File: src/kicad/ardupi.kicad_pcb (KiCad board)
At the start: 2 copper layers, 65 x 56 mm, 54 parts, among them J1 GPIO, J10 Conn_01x04, J11 TSW-108-08-L-T-RA, J2 Conn_01x10, J3 Conn_01x05, J4 Conn_01x04, J6 Conn_01x05, J7 Conn_01x06, J8 Conn_01x04, J9 Conn_01x02, U1 CAT24C256, U2 ULN2803ADW, U3 PCA9685BS, U4 ADS1115IRUGR, U5 MPU-9250, U6 BMP280

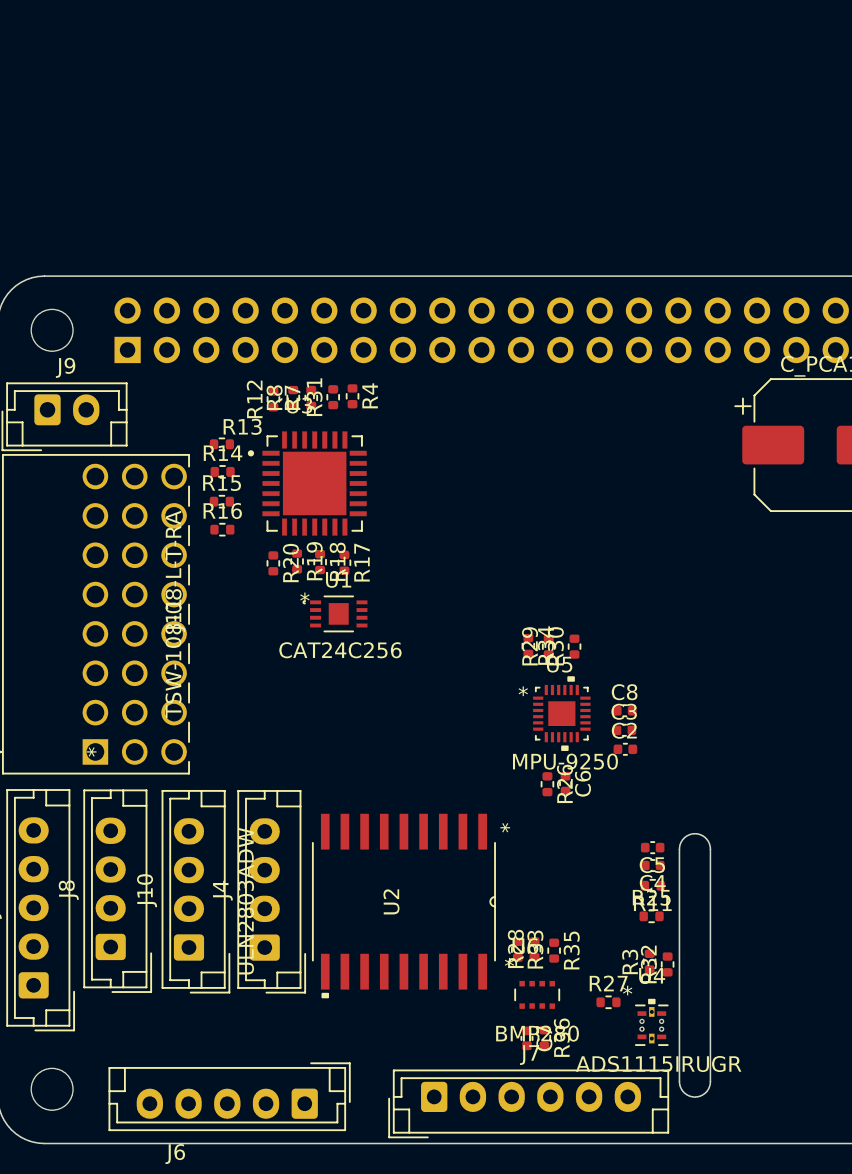
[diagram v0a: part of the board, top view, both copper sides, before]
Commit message: +ADS1115IDGSR update all symbol footprints VSS = GND
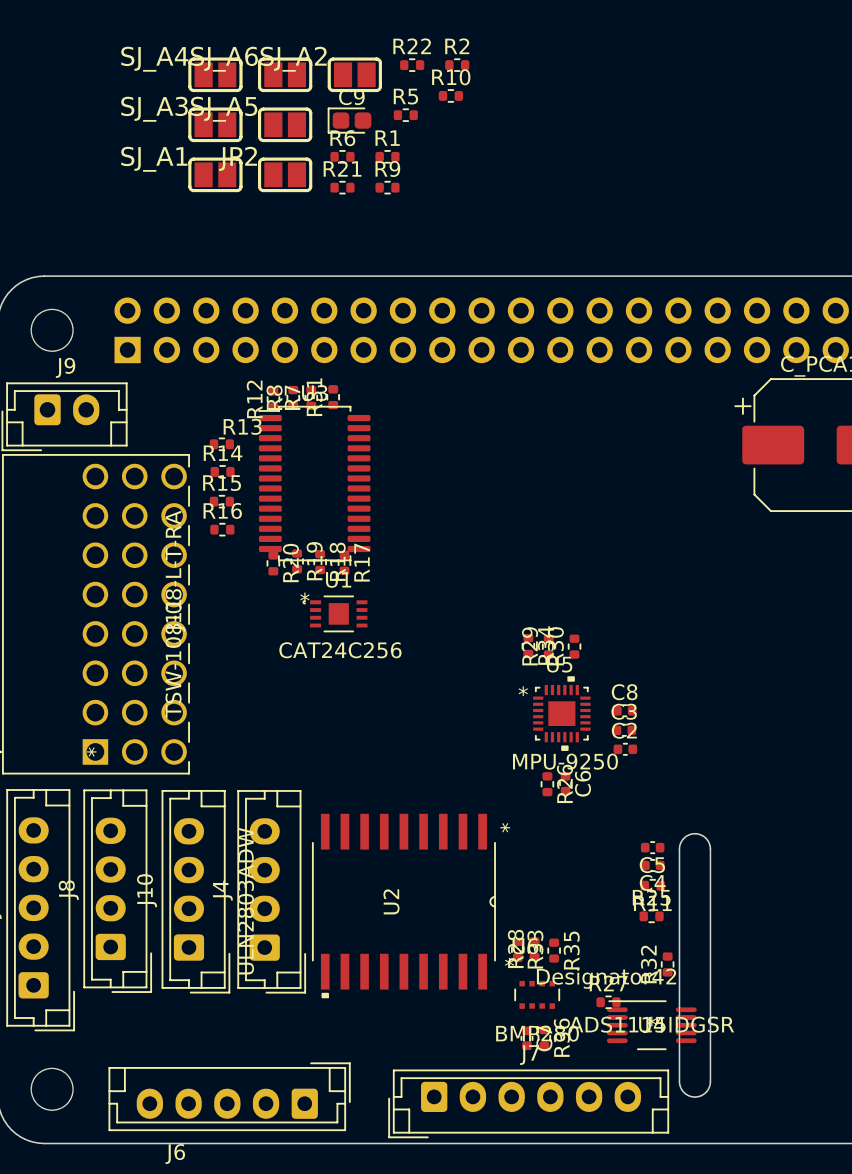
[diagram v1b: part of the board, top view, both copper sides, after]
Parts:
- removed R3, R4: 10k, Resistor_SMD:R_0402_1005Metric
- added C9: 100n, Capacitor_Tantalum_SMD:CP_EIA-1608-10_AVX-L, F.Cu at (122.9, 34.0)
- added JP2: ID_WP, Ardupi:SOLDERJUMPER_REFLOW_NOPASTE, F.Cu at (118.5, 37.5)
- added R1: 10k, Resistor_SMD:R_0402_1005Metric, F.Cu at (125.2, 36.3)
- added R10: 10k, Resistor_SMD:R_0402_1005Metric, F.Cu at (129.2, 32.4)
- added R2: 10k, Resistor_SMD:R_0402_1005Metric, F.Cu at (129.7, 30.4)
- added R21: 3.9k, Resistor_SMD:R_0402_1005Metric, F.Cu at (122.2, 38.3)
- added R22: 3.9k, Resistor_SMD:R_0402_1005Metric, F.Cu at (126.7, 30.4)
- added R5: 10k, Resistor_SMD:R_0402_1005Metric, F.Cu at (126.3, 33.6)
- added R6: 10K, Resistor_SMD:R_0402_1005Metric, F.Cu at (122.2, 36.3)
- added R9: 10k, Resistor_SMD:R_0402_1005Metric, F.Cu at (125.2, 38.3)
- added SJ_A1: SOLDERJUMPERREFLOW_NOPASTE, Ardupi:SOLDERJUMPER_REFLOW_NOPASTE, F.Cu at (114.0, 37.5)
- added SJ_A2: SOLDERJUMPERREFLOW_NOPASTE, Ardupi:SOLDERJUMPER_REFLOW_NOPASTE, F.Cu at (123.0, 31.0)
- added SJ_A3: SOLDERJUMPERREFLOW_NOPASTE, Ardupi:SOLDERJUMPER_REFLOW_NOPASTE, F.Cu at (114.0, 34.2)
- added SJ_A4: SOLDERJUMPERREFLOW_NOPASTE, Ardupi:SOLDERJUMPER_REFLOW_NOPASTE, F.Cu at (114.0, 31.0)
- added SJ_A5: SOLDERJUMPERREFLOW_NOPASTE, Ardupi:SOLDERJUMPER_REFLOW_NOPASTE, F.Cu at (118.5, 34.2)
- added SJ_A6: SOLDERJUMPERREFLOW_NOPASTE, Ardupi:SOLDERJUMPER_REFLOW_NOPASTE, F.Cu at (118.5, 31.0)
- J1: value GPIO -> RPI-4B-Header
- U3: value PCA9685BS -> PCA9685PW; footprint Ardupi:PCA9685BS_118 -> Package_SO:TSSOP-28_4.4x9.7mm_P0.65mm
- U4: value ADS1115IRUGR -> ADS1115IDGSR; footprint Ardupi:ADS1115IRUGT -> Ardupi:ADS1115IDGSR
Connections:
- J1 pad 27: /ID_SDA -> unconnected-(J1-Pad27)
- J1 pad 28: /ID_SCL -> unconnected-(J1-Pad28)
- R32 pad 1: /SDA1 -> +5V
- R32 pad 2: +5V -> /SDA1
- U3 pad 1: unconnected-(U3-Pad1) -> Net-(R5-Pad1)
- U3 pad 10: /PWM7 -> /PWM5
- U3 pad 11: unconnected-(U3-Pad11) -> /PWM6
- U3 pad 12: /PWM8 -> /PWM7
- U3 pad 13: /PWM9 -> /PWM8
- U3 pad 14: /PWM10 -> GND
- U3 pad 15: /PWM11 -> /PWM9
- U3 pad 16: /PWM12 -> /PWM10
- U3 pad 17: /PWM13 -> /PWM11
- U3 pad 18: /PWM14 -> /PWM12
- U3 pad 19: /PWM15 -> /PWM13
- U3 pad 2: unconnected-(U3-Pad2) -> Net-(R6-Pad1)
- U3 pad 20: unconnected-(U3-Pad20) -> /PWM14
- U3 pad 21: unconnected-(U3-Pad21) -> /PWM15
- U3 pad 22: /SCL1 -> /PWM16
- U3 pad 23: Net-(R7-Pad1) -> /PCA_EN
- U3 pad 24: Net-(R8-Pad1) -> Net-(R10-Pad1)
- U3 pad 25: unconnected-(U3-Pad25) -> GND
- U3 pad 26: /PCA_EN -> /SCL1
- U3 pad 27: unconnected-(U3-Pad27) -> /SDA1
- U3 pad 28: unconnected-(U3-Pad28) -> +5V
- U3 pad 3: unconnected-(U3-Pad3) -> Net-(R7-Pad1)
- U3 pad 4: /PWM1 -> Net-(R8-Pad1)
- U3 pad 5: /PWM2 -> Net-(R9-Pad1)
- U3 pad 6: /PWM3 -> /PWM1
- U3 pad 7: /PWM4 -> /PWM2
- U3 pad 8: /PWM5 -> /PWM3
- U3 pad 9: /PWM6 -> /PWM4
- U4 pad 10: /SCL1 -> /AIO2
- U4 pad 6: /AIO2 -> /SCL1
- U4 pad 9: /SDA1 -> /AIO3
- U5 pad 18: unconnected-(U5-Pad18) -> GND

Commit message: schematic version bump
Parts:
- U1: value CAT24C256 -> CAT24C256HU4IGT3
- U2: value ULN2803ADW -> ULN2803ADWR
- U3: footprint Package_SO:TSSOP-28_4.4x9.7mm_P0.65mm -> Ardupi:PCA9685PW_118
- moved SJ_A2 158.3 mm to (39.6, 165.6)
- moved R10 155.4 mm to (53.2, 167.9)
- moved C9 155.2 mm to (43.9, 167.6)
- moved R21 154.4 mm to (38.8, 168.2)
- moved R1 151.4 mm to (50.3, 167.9)
- moved R5 146.4 mm to (64.9, 166.5)
- moved SJ_A4 144.2 mm to (53.9, 162.0)
- moved JP2 143.2 mm to (53.9, 165.3)
- moved R8 135.8 mm to (47.4, 167.3), turned to 0 degrees
- moved J2 135.2 mm to (33.5, 126.2), turned to 0 degrees
- moved U4 131.3 mm to (33.7, 166.3)
- moved R22 130.0 mm to (78.5, 151.1)
- moved R9 129.8 mm to (69.5, 155.6)
- moved U3 129.7 mm to (36.4, 156.2)
- moved J9 124.5 mm to (45.6, 163.1)
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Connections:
- J1 pad 1: +3V3 -> unconnected-(J1-Pad1)
- J1 pad 11: /SRVO_EN -> unconnected-(J1-Pad11)
- J1 pad 13: /LED1 -> unconnected-(J1-Pad13)
- J1 pad 15: /LED2 -> unconnected-(J1-Pad15)
- J1 pad 17: +3V3 -> unconnected-(J1-Pad17)
- J1 pad 19: /SPI_MOSI -> unconnected-(J1-Pad19)
- J1 pad 21: /SPI_MISO -> unconnected-(J1-Pad21)
- J1 pad 23: /SPI_SCLK -> unconnected-(J1-Pad23)
- J1 pad 25: GND -> unconnected-(J1-Pad25)
- J1 pad 28: unconnected-(J1-Pad28) -> /ID_SCL
- J1 pad 29: /RC1 -> unconnected-(J1-Pad29)
- J1 pad 3: /SDA1 -> unconnected-(J1-Pad3)
- J1 pad 31: /RC2 -> unconnected-(J1-Pad31)
- J1 pad 33: /RC3 -> unconnected-(J1-Pad33)
- J1 pad 35: /RC4 -> unconnected-(J1-Pad35)
- J1 pad 37: /RC5 -> unconnected-(J1-Pad37)
- J1 pad 39: GND -> unconnected-(J1-Pad39)
- J1 pad 5: /SCL1 -> unconnected-(J1-Pad5)
- J1 pad 7: /LED3 -> unconnected-(J1-Pad7)
- J1 pad 9: GND -> unconnected-(J1-Pad9)

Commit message: +NEO-M8Q-01A module
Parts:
- removed C2, C6: 0.1uF, Capacitor_SMD:C_0402_1005Metric
- removed C3, C4, C8: 1uF, Capacitor_SMD:C_0402_1005Metric
- removed C5: 0.1uf, Capacitor_SMD:C_0402_1005Metric
- removed C7: 0.01uF, Capacitor_SMD:C_0402_1005Metric
- removed C9: 100n, Capacitor_Tantalum_SMD:CP_EIA-1608-10_AVX-L
- removed C_PCA1: 10uF, Capacitor_SMD:CP_Elec_8x5.4
- removed J10, J4, J8: Conn_01x04, Connector_JST:JST_EH_B4B-EH-A_1x04_P2.50mm_Vertical
- removed J11: TSW-108-08-L-T-RA, Ardupi:TSW-108-08-L-T-RA
- removed J2: Conn_01x10, Connector_JST:JST_EH_B10B-EH-A_1x10_P2.50mm_Vertical
- removed J3, J6: Conn_01x05, Connector_JST:JST_EH_B5B-EH-A_1x05_P2.50mm_Vertical
- removed J7: Conn_01x06, Connector_JST:JST_EH_B6B-EH-A_1x06_P2.50mm_Vertical
- removed J9: Conn_01x02, Connector_JST:JST_EH_B2B-EH-A_1x02_P2.50mm_Vertical
- removed JP2: ID_WP, Ardupi:SOLDERJUMPER_REFLOW_NOPASTE
- removed R1, R10, R2, R5, R9: 10k, Resistor_SMD:R_0402_1005Metric
- removed R11, R6, R7, R8: 10K, Resistor_SMD:R_0402_1005Metric
- removed R12: 460, Resistor_SMD:R_0402_1005Metric
- removed R13, R14, R15, R16, R17, R18, R19, R20: 220 Ω, Resistor_SMD:R_0402_1005Metric
- removed R21, R22: 3.9k, Resistor_SMD:R_0402_1005Metric
- removed R25, R26, R27, R28, R31, R32, R36: 10KΩ, Resistor_SMD:R_0402_1005Metric
- removed R29, R30, R33, R34, R35: 4.7KΩ, Resistor_SMD:R_0402_1005Metric
- removed SJ_A1, SJ_A2, SJ_A3, SJ_A4, SJ_A5, SJ_A6: SOLDERJUMPERREFLOW_NOPASTE, Ardupi:SOLDERJUMPER_REFLOW_NOPASTE
- removed U1: CAT24C256HU4IGT3, Ardupi:CAT24C256HU4IGT3
- removed U2: ULN2803ADWR, Ardupi:ULN2803ADWR
- removed U3: PCA9685PW, Ardupi:PCA9685PW_118
- removed U4: ADS1115IDGSR, Ardupi:ADS1115IDGSR
- removed U5: MPU-9250, Ardupi:mpu9250
- removed U6: BMP280, Ardupi:bmp280
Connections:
- J1 pad 1: unconnected-(J1-Pad1) -> +3V3
- J1 pad 11: unconnected-(J1-Pad11) -> /SRVO_EN
- J1 pad 13: unconnected-(J1-Pad13) -> /LED1
- J1 pad 15: unconnected-(J1-Pad15) -> /LED2
- J1 pad 17: unconnected-(J1-Pad17) -> +3V3
- J1 pad 19: unconnected-(J1-Pad19) -> /SPI_MOSI
- J1 pad 21: unconnected-(J1-Pad21) -> /SPI_MISO
- J1 pad 23: unconnected-(J1-Pad23) -> /SPI_SCLK
- J1 pad 25: unconnected-(J1-Pad25) -> GND
- J1 pad 27: unconnected-(J1-Pad27) -> /ID_SD
- J1 pad 28: /ID_SCL -> /ID_SC
- J1 pad 29: unconnected-(J1-Pad29) -> /RC1
- J1 pad 3: unconnected-(J1-Pad3) -> /SDA1
- J1 pad 31: unconnected-(J1-Pad31) -> /RC2
- J1 pad 33: unconnected-(J1-Pad33) -> /RC3
- J1 pad 35: unconnected-(J1-Pad35) -> /RC4
- J1 pad 37: unconnected-(J1-Pad37) -> /RC5
- J1 pad 39: unconnected-(J1-Pad39) -> GND
- J1 pad 5: unconnected-(J1-Pad5) -> /SCL1
- J1 pad 7: unconnected-(J1-Pad7) -> /LED3
- J1 pad 9: unconnected-(J1-Pad9) -> GND

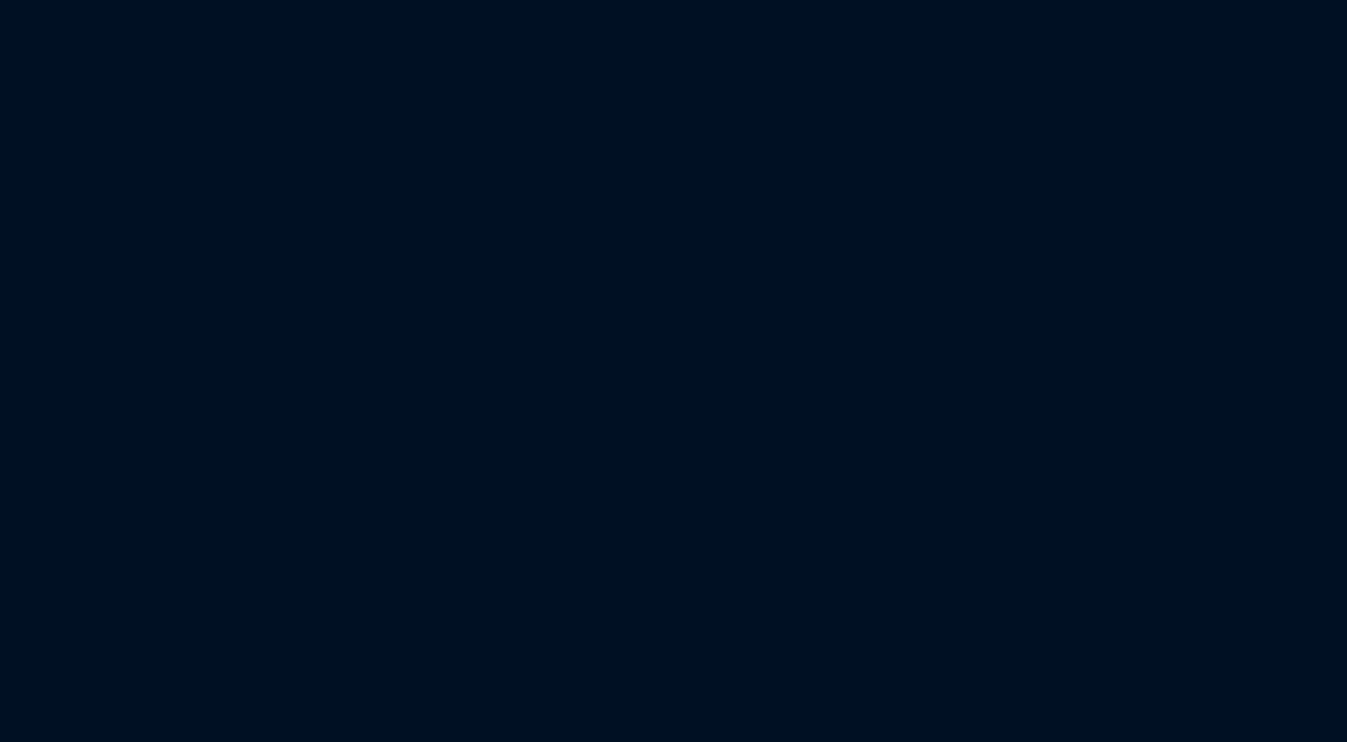
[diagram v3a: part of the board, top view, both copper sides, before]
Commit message: + expresslrs.
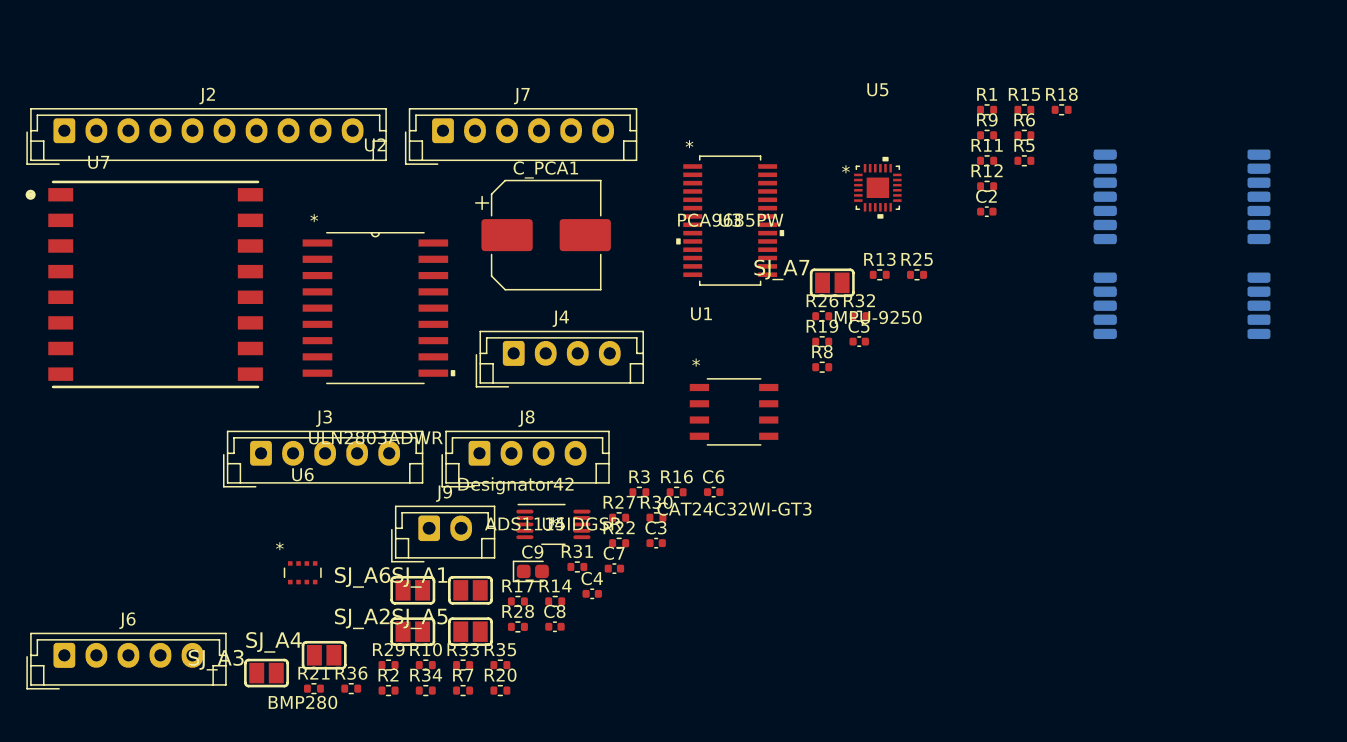
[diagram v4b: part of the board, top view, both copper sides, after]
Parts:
- added C2: 0.1uF, Capacitor_SMD:C_0402_1005Metric, F.Cu at (112.7, 133.0)
- added C3: 1uF, Capacitor_SMD:C_0402_1005Metric, F.Cu at (86.9, 158.9)
- added C4: 1uF, Capacitor_SMD:C_0402_1005Metric, F.Cu at (81.9, 162.8)
- added C5: 0.1uf, Capacitor_SMD:C_0402_1005Metric, F.Cu at (102.7, 143.2)
- added C6: 0.1uF, Capacitor_SMD:C_0402_1005Metric, F.Cu at (91.4, 154.9)
- added C7: 0.01uF, Capacitor_SMD:C_0402_1005Metric, F.Cu at (83.6, 160.9)
- added C8: 1uF, Capacitor_SMD:C_0402_1005Metric, F.Cu at (79.0, 165.4)
- added C9: 100n, Capacitor_Tantalum_SMD:CP_EIA-1608-10_AVX-L, F.Cu at (77.3, 161.1)
- added C_PCA1: 10uF, Capacitor_SMD:CP_Elec_8x5.4, F.Cu at (78.3, 134.8)
- added J2: Conn_01x10, Connector_JST:JST_EH_B10B-EH-A_1x10_P2.50mm_Vertical, F.Cu at (40.7, 126.7)
- added J3: Conn_01x05, Connector_JST:JST_EH_B5B-EH-A_1x05_P2.50mm_Vertical, F.Cu at (56.0, 151.9)
- added J4: Conn_01x04, Connector_JST:JST_EH_B4B-EH-A_1x04_P2.50mm_Vertical, F.Cu at (75.8, 144.1)
- added J6: Conn_01x05, Connector_JST:JST_EH_B5B-EH-A_1x05_P2.50mm_Vertical, F.Cu at (40.7, 167.7)
- added J7: Conn_01x06, Connector_JST:JST_EH_B6B-EH-A_1x06_P2.50mm_Vertical, F.Cu at (70.2, 126.7)
- added J8: Conn_01x04, Connector_JST:JST_EH_B4B-EH-A_1x04_P2.50mm_Vertical, F.Cu at (73.1, 151.9)
- added J9: Conn_01x02, Connector_JST:JST_EH_B2B-EH-A_1x02_P2.50mm_Vertical, F.Cu at (69.2, 157.7)
- added M1: NEO-M8Q-01A, Ardupi:ublox_NEO, B.Cu at (127.9, 135.6)
- added R1: 10k, Resistor_SMD:R_0402_1005Metric, F.Cu at (112.7, 125.1)
- added R10: 10k, Resistor_SMD:R_0402_1005Metric, F.Cu at (68.9, 168.4)
- added R11: 10K, Resistor_SMD:R_0402_1005Metric, F.Cu at (112.7, 129.1)
- added R12: 460, Resistor_SMD:R_0402_1005Metric, F.Cu at (112.7, 131.0)
- added R13: 220 Ω, Resistor_SMD:R_0402_1005Metric, F.Cu at (104.3, 137.9)
- added R14: 220 Ω, Resistor_SMD:R_0402_1005Metric, F.Cu at (79.0, 163.4)
- added R15: 220 Ω, Resistor_SMD:R_0402_1005Metric, F.Cu at (115.6, 125.1)
- added R16: 220 Ω, Resistor_SMD:R_0402_1005Metric, F.Cu at (88.5, 154.9)
- added R17: 220 Ω, Resistor_SMD:R_0402_1005Metric, F.Cu at (76.1, 163.4)
- added R18: 220 Ω, Resistor_SMD:R_0402_1005Metric, F.Cu at (118.5, 125.1)
- added R19: 220 Ω, Resistor_SMD:R_0402_1005Metric, F.Cu at (99.8, 143.2)
- added R2: 10k, Resistor_SMD:R_0402_1005Metric, F.Cu at (66.0, 170.4)
- added R20: 220 Ω, Resistor_SMD:R_0402_1005Metric, F.Cu at (74.7, 170.4)
- added R21: 3.9k, Resistor_SMD:R_0402_1005Metric, F.Cu at (60.2, 170.2)
- added R22: 3.9k, Resistor_SMD:R_0402_1005Metric, F.Cu at (84.0, 158.9)
- added R25: 10KΩ, Resistor_SMD:R_0402_1005Metric, F.Cu at (107.2, 137.9)
- added R26: 10KΩ, Resistor_SMD:R_0402_1005Metric, F.Cu at (99.8, 141.2)
- added R27: 10KΩ, Resistor_SMD:R_0402_1005Metric, F.Cu at (84.0, 156.9)
- added R28: 10KΩ, Resistor_SMD:R_0402_1005Metric, F.Cu at (76.1, 165.4)
- added R29: 4.7KΩ, Resistor_SMD:R_0402_1005Metric, F.Cu at (66.0, 168.4)
- added R3: 1k, Resistor_SMD:R_0402_1005Metric, F.Cu at (85.6, 154.9)
- added R30: 4.7KΩ, Resistor_SMD:R_0402_1005Metric, F.Cu at (86.9, 156.9)
- added R31: 10KΩ, Resistor_SMD:R_0402_1005Metric, F.Cu at (80.7, 160.8)
- added R32: 10KΩ, Resistor_SMD:R_0402_1005Metric, F.Cu at (102.8, 141.2)
- added R33: 4.7KΩ, Resistor_SMD:R_0402_1005Metric, F.Cu at (71.8, 168.4)
- added R34: 4.7KΩ, Resistor_SMD:R_0402_1005Metric, F.Cu at (68.9, 170.4)
- added R35: 4.7KΩ, Resistor_SMD:R_0402_1005Metric, F.Cu at (74.7, 168.4)
- added R36: 10KΩ, Resistor_SMD:R_0402_1005Metric, F.Cu at (63.1, 170.2)
- added R5: 10k, Resistor_SMD:R_0402_1005Metric, F.Cu at (115.6, 129.1)
- added R6: 10K, Resistor_SMD:R_0402_1005Metric, F.Cu at (115.6, 127.1)
- added R7: 10K, Resistor_SMD:R_0402_1005Metric, F.Cu at (71.8, 170.4)
- added R8: 10K, Resistor_SMD:R_0402_1005Metric, F.Cu at (99.8, 145.2)
- added R9: 10k, Resistor_SMD:R_0402_1005Metric, F.Cu at (112.7, 127.1)
- added SJ_A1: SOLDERJUMPERREFLOW_NOPASTE, Ardupi:SOLDERJUMPER_REFLOW_NOPASTE, F.Cu at (72.4, 162.6)
- added SJ_A2: SOLDERJUMPERREFLOW_NOPASTE, Ardupi:SOLDERJUMPER_REFLOW_NOPASTE, F.Cu at (67.9, 165.8)
- added SJ_A3: SOLDERJUMPERREFLOW_NOPASTE, Ardupi:SOLDERJUMPER_REFLOW_NOPASTE, F.Cu at (56.5, 169.0)
- added SJ_A4: SOLDERJUMPERREFLOW_NOPASTE, Ardupi:SOLDERJUMPER_REFLOW_NOPASTE, F.Cu at (61.0, 167.6)
- added SJ_A5: SOLDERJUMPERREFLOW_NOPASTE, Ardupi:SOLDERJUMPER_REFLOW_NOPASTE, F.Cu at (72.4, 165.8)
- added SJ_A6: SOLDERJUMPERREFLOW_NOPASTE, Ardupi:SOLDERJUMPER_REFLOW_NOPASTE, F.Cu at (67.9, 162.6)
- added SJ_A7: SOLDERJUMPERREFLOW_NOPASTE, Ardupi:SOLDERJUMPER_REFLOW_NOPASTE, F.Cu at (100.6, 138.6)
- added U1: CAT24C32WI-GT3, Ardupi:CAT24C32WI-GT3, F.Cu at (93.0, 148.6)
- added U2: ULN2803ADWR, Ardupi:ULN2803ADWR, F.Cu at (65.0, 140.5)
- added U3: PCA9685PW, Ardupi:PCA9685PW_118, F.Cu at (92.7, 133.7)
- added U4: ADS1115IDGSR, Ardupi:ADS1115IDGSR, F.Cu at (78.9, 157.4)
- added U5: MPU-9250, Ardupi:mpu9250, F.Cu at (104.2, 131.2)
- added U6: BMP280, Ardupi:bmp280, F.Cu at (59.3, 161.2)
- added U7: RFM95W-868S2, Ardupi:RFM95W-868S2, F.Cu at (47.8, 138.7)

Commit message: fix
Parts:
- M1: moved to F.Cu
- turned M1 to 0 degrees
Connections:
- U7 pad 1: unconnected-(U7-Pad1) -> GND
- U7 pad 10: unconnected-(U7-Pad10) -> GND
- U7 pad 13: unconnected-(U7-Pad13) -> +3V3
- U7 pad 8: unconnected-(U7-Pad8) -> GND
